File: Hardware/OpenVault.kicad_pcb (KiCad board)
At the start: 4 copper layers, 45 x 54.7 mm, 58 parts, among them IC1 NPM1300-QEAA-R, IC2 STM32WB5MMGH6TR, IC3 TROPIC01, J03 HC-FPC-05-09-24RLTAG, J1 USB_C_Receptacle_USB2.0_16P, J2 Conn_01x02_Socket, J4 JUSHUO AFC01-S06FCC-00, J5 TC2030, Q1 Si1308EDL, SW2 SKSCLBE010, U1 USBLC6-2SC6, U3 W25Q128JVS

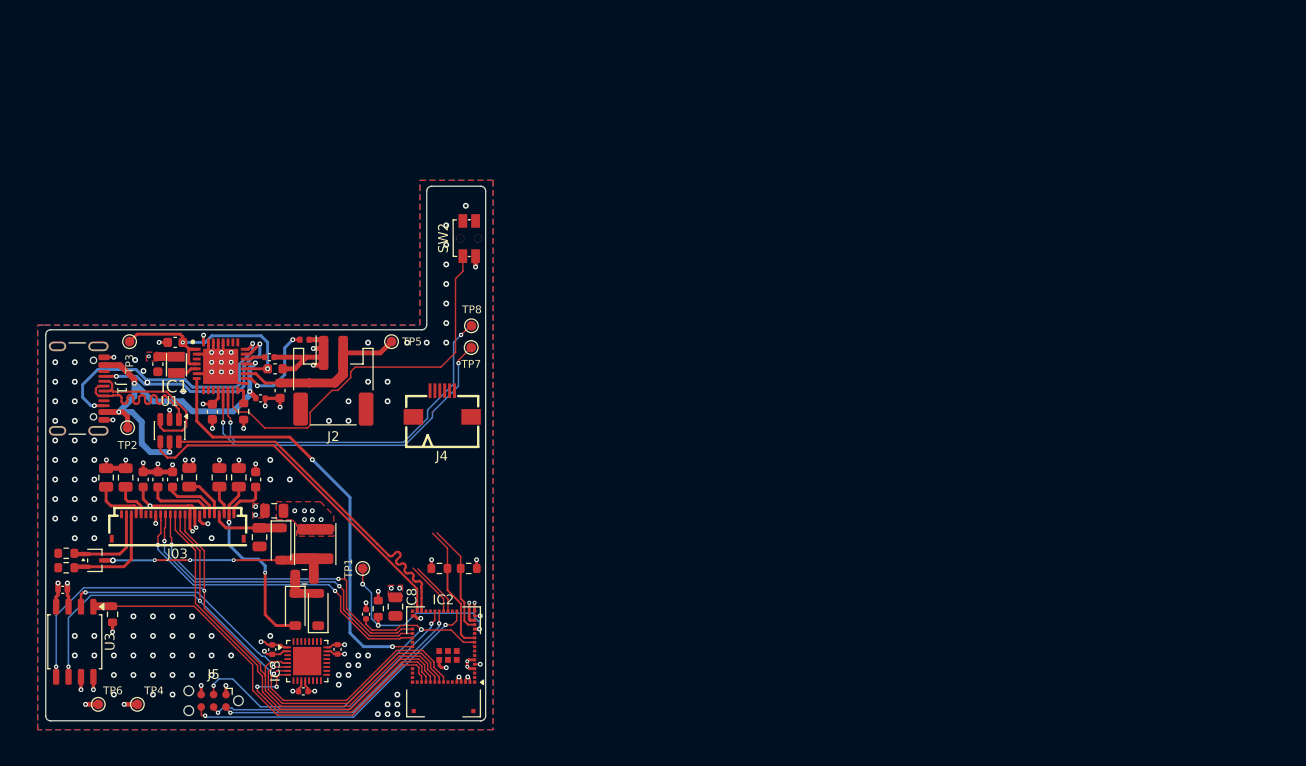
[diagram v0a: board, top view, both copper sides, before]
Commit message: Add VSON-8 3D model and production files
Add a STEP 3D model and KiCad footprint for the VSON-8 package, plus a Vias directory. Add production outputs (Hardware/production/V3.zip, V3_bom.csv, V3_designators.csv, V3_positions.csv) and update Hardware/production/netlist.ipc. Update KiCad project files (Hardware/OpenVault.kicad_pcb, .kicad_pro, .kicad_sch, and Symbols/OpenVaultSymbols.kicad_sym) and adjust fabrication-toolkit-options.json to include the new artifacts.
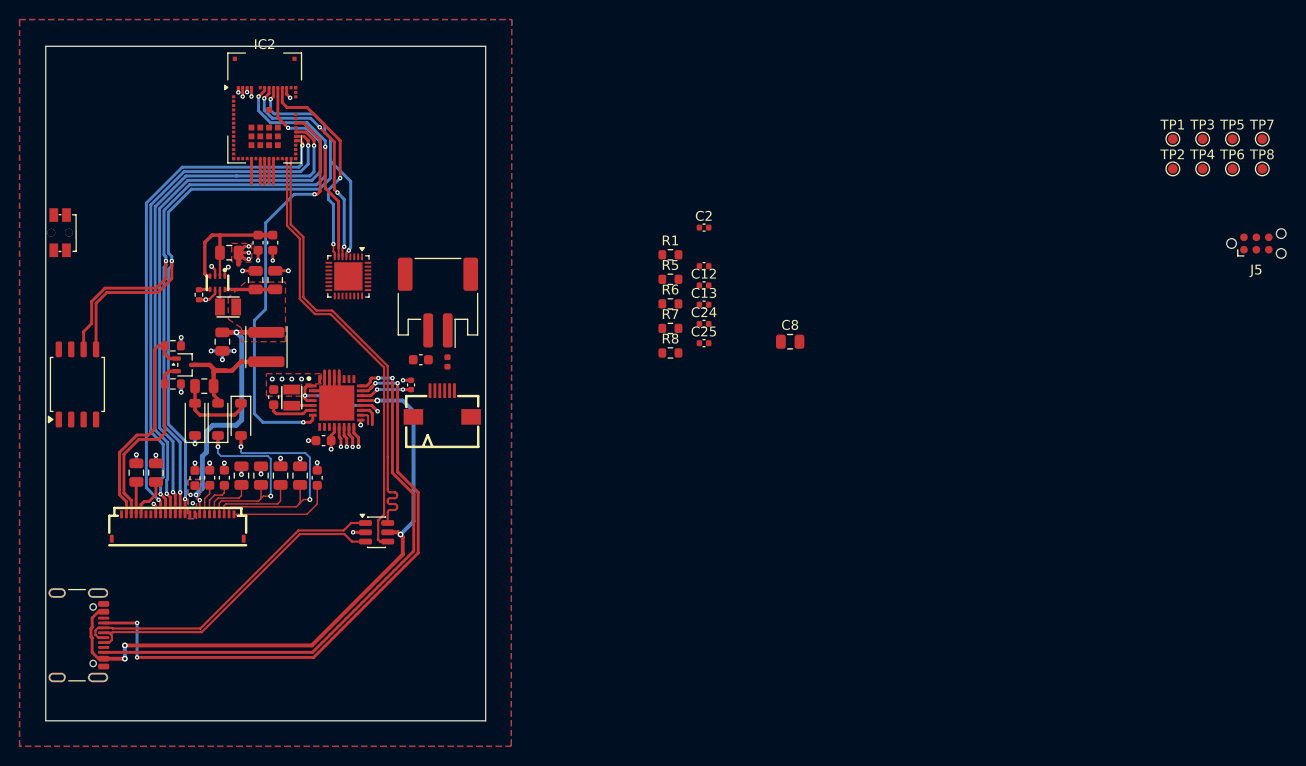
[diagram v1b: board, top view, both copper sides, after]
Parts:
- added C26: 4u7, Capacitor_SMD:C_0805_2012Metric, F.Cu at (137.8, 72.8)
- added C27: 22uF/25V, Capacitor_SMD:C_0805_2012Metric, F.Cu at (140.5, 75.6)
- added C28: 22uF/25V, Capacitor_SMD:C_0805_2012Metric, F.Cu at (142.5, 75.6)
- added L3: 2.2uH, OpenVaultFootprints:IND-SMD_L2.0-W1.6, F.Cu at (137.7, 78.3)
- added R4: 267K, Resistor_SMD:R_0402_1005Metric, F.Cu at (134.7, 77.1)
- added U2: TPS62840DLCR, OpenVaultFootprints:VSON-8_L2.0-W1.5-P0.50-BL, F.Cu at (136.6, 75.9)
- R6, R7: value 4R7 -> 4.7K
- moved TP6 128.3 mm to (240.4, 64.2)
- moved TP4 122.0 mm to (237.4, 64.2)
- moved J5 116.5 mm to (242.9, 71.9), turned to 0 degrees
- moved TP3 111.7 mm to (237.4, 61.2)
- moved TP2 110.2 mm to (234.3, 64.2)
- moved TP1 93.8 mm to (234.3, 61.2)
- moved TP5 88.5 mm to (240.4, 61.2)
- moved TP7 83.7 mm to (243.5, 61.2)
- moved TP8 82.5 mm to (243.5, 64.2)
- moved C25 70.3 mm to (186.4, 82.1), turned to 0 degrees
- moved R5 66.6 mm to (182.9, 75.5), turned to 0 degrees
- moved IC2 59.5 mm to (141.4, 58.0), turned to 0 degrees
- moved C12 58.4 mm to (186.4, 76.1)
- moved C13 56.5 mm to (186.4, 78.1), turned to 0 degrees
- moved C11 54.2 mm to (186.4, 74.2), turned to 0 degrees
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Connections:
- C17 pad 2: +3V3 -> +3V3_EINK
- C9 pad 1: +3V3 -> +3V3_EINK
- IC2 pad 35: /D/C -> /BUSY
- IC2 pad 37: /BUSY -> /D/C
- J03 pad 15: +3V3 -> +3V3_EINK
- J03 pad 16: +3V3 -> +3V3_EINK
- L2 pad 1: +3V3 -> +3V3_EINK
- U1 pad 1: USBD+ -> USBD-
- U1 pad 3: USBD- -> USBD+
- U1 pad 4: P_USBD- -> P_USBD+
- U1 pad 6: P_USBD+ -> P_USBD-
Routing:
- net I2C1_SDA: track 49.5 -> 2.17 mm, vias 2 -> 1
- net I2C1_SCL: track 49.0 -> 2.14 mm, vias 2 -> 1
- net FLASH_CSN: track 43.3 -> 1.19 mm, vias 0 -> 1
- net CC1: track 22.4 -> 64.1 mm, vias 2 -> 4
- net SWD_RESET: track 39.8 -> 0.00 mm, vias 2 -> 0
- net +3V3: track 41.7 -> 2.42 mm, vias 30 -> 5
- net SHPHLD: track 39.9 -> 2.19 mm, vias 0 -> 1
- net CC2: track 27.3 -> 58.3 mm
- net +3V3_EINK: track 0.00 -> 29.8 mm, vias 0 -> 4
- net SWD_O: track 32.1 -> 2.60 mm, vias 2 -> 0
- net MCU_SPI_MISO: track 50.4 -> 23.3 mm, vias 2 -> 4
- net SWD_CLK: track 28.1 -> 2.60 mm, vias 2 -> 0
- net MCU_SPI_SCK: track 66.4 -> 91.6 mm, vias 3 -> 4
- net SWD_IO: track 27.3 -> 2.58 mm, vias 2 -> 0
- net VBUS: track 40.2 -> 65.0 mm, vias 5 -> 4
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- added copper zone on B.Cu, net +3V3_EINK
- added copper zone on F.Cu, net +3V3_EINK
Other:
- board size 45 x 54.7 mm -> 45 x 69 mm
- board text removed: "Labs"
- board text removed: "Nocta"
- board text removed: "OpenVault V1"

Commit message: V4
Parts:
- removed TH1: NTC 10K, Inductor_SMD:L_0402_1005Metric
- IC1: footprint SamacSys_Parts:QFN50P500X500X90-33N -> Package_DFN_QFN:QFN-32-1EP_5x5mm_P0.5mm_EP3.45x3.45mm_ThermalVias
- J2: value Conn_01x02_Socket -> BATT_CON; footprint Connector_JST:JST_PH_S2B-PH-SM4-TB_1x02-1MP_P2.00mm_Horizontal -> Connector_JST:JST_SH_SM03B-SRSS-TB_1x03-1MP_P1.00mm_Horizontal
- moved J5 119.0 mm to (125.2, 54.1), turned to 180 degrees
- moved TP1 103.2 mm to (131.1, 62.9)
- moved TP5 97.4 mm to (145.0, 80.8)
- moved TP2 94.9 mm to (149.2, 106.2)
- moved TP8 94.9 mm to (159.6, 108.6)
- moved TP7 92.1 mm to (153.5, 80.8), turned to 180 degrees
- moved TP6 85.7 mm to (160.7, 95.6)
- moved TP4 76.3 mm to (162.2, 77.5)
- moved TP3 76.3 mm to (162.2, 74.1)
- moved R6 64.8 mm to (120.4, 92.5), turned to 90 degrees
- moved C15 63.7 mm to (123.4, 91.5)
- moved C11 62.2 mm to (136.5, 61.3), turned to 90 degrees
- moved C12 54.0 mm to (136.6, 59.1), turned to 180 degrees
- moved R3 52.9 mm to (134.8, 61.2), turned to -90 degrees
- moved C3 48.0 mm to (153.3, 105.0), turned to 135 degrees
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- renumbered C26 to C1, C7 to C10, C8 to C11, C24 to C12, C9 to C13, C10 to C14, C25 to C15, C11 to C16, C12 to C17, C13 to C18, C14 to C19, C1 to C2, C15 to C20, C16 to C21, C17 to C22, C19 to C23, C21 to C24, C22 to C25, C23 to C26, C20 to C27, C18 to C28, C2 to C3, C27 to C4, C3 to C5, C28 to C6, C4 to C7, C5 to C8, C6 to C9, J03 to J04, J4 to J3, L3 to L1, L1 to L2, L2 to L3, R4 to R2, R8 to R3, R6 to R4, R7 to R5, R5 to R6, R2 to R7, R3 to R8, SW2 to SW1
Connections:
- IC1 pad 1: VSYS -> unconnected-(IC1-VOUT1-Pad1)
- J2 pad 2: VBAT -> NTC
- TP3 pad 1: VSYS -> I2C1_SDA
- TP4 pad 1: +3V3 -> I2C1_SCL
- TP5 pad 1: VBAT -> VSYS
- TP6 pad 1: GND -> +3V3
- TP7 pad 1: I2C1_SDA -> VBAT
- TP8 pad 1: I2C1_SCL -> GND
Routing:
- net FLASH_CSN: track 1.19 -> 80.8 mm, vias 1 -> 2
- net I2C1_SDA: track 2.17 -> 80.0 mm, vias 1 -> 4
- net I2C1_SCL: track 2.14 -> 78.9 mm, vias 1 -> 4
- net SHPHLD: track 2.19 -> 71.9 mm, vias 1 -> 2
- net MCU_SPI_MISO: track 23.3 -> 68.0 mm, vias 4 -> 5
- net VSYS: track 28.1 -> 68.8 mm, vias 2 -> 5
- net TOUCH_RST: track 2.60 -> 37.4 mm, vias 0 -> 2
- net TOUCH_INT: track 2.62 -> 37.4 mm, vias 0 -> 2
- net GND: track 53.0 -> 87.1 mm, vias 36 -> 154
- net +3V3: track 2.42 -> 32.8 mm, vias 5 -> 21
- net SWD_CLK: track 2.60 -> 31.8 mm, vias 0 -> 2
- net SWD_IO: track 2.58 -> 31.0 mm, vias 0 -> 2
- net SWD_O: track 2.60 -> 28.7 mm
- net NTC: track 1.66 -> 26.4 mm, vias 0 -> 2
- net /PREVGL: track 24.5 -> 0.00 mm, vias 2 -> 0
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- removed copper zone on B.Cu, net +3V3_EINK
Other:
- board text added: "Labs"
- board text added: "Nocta"
- board text added: "OpenVault V2"

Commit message: Update OpenVault.kicad_pcb
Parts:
- removed TP3, TP4: TestPoint, TestPoint:TestPoint_Pad_D1.0mm
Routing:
- net MCU_SPI_MOSI: track 80.6 -> 14.9 mm, vias 3 -> 2
- net MCU_SPI_SCK: track 81.9 -> 16.4 mm, vias 3 -> 1
- net SHPHLD: track 71.9 -> 10.5 mm
- net /D/C: track 46.9 -> 2.22 mm, vias 1 -> 0
- net DISPLAY_CSN: track 52.8 -> 8.40 mm
- net MCU_SPI_MISO: track 68.0 -> 23.7 mm, vias 5 -> 3
- net I2C1_SDA: track 80.0 -> 37.2 mm, vias 4 -> 2
- net /RES: track 45.4 -> 3.87 mm
- net /BUSY: track 44.3 -> 3.02 mm
- net FLASH_CSN: track 80.8 -> 43.7 mm
- net I2C1_SCL: track 78.9 -> 50.0 mm, vias 4 -> 3
- net SWD_CLK: track 31.8 -> 9.81 mm, vias 2 -> 0
- net SWD_IO: track 31.0 -> 10.7 mm, vias 2 -> 0
- net SWD_O: track 28.7 -> 8.43 mm
- net /GDR_INK: track 11.5 -> 2.20 mm
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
